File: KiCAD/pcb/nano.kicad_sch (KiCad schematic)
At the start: 24 parts, among them J1 Barrel_Jack_Switch, J2 Conn_01x02_Male, J3 Conn_01x02_Male, J4 Conn_01x04_Male, J5 Conn_01x03_Male, K1 SANYOU_SRD_Form_C, K2 SANYOU_SRD_Form_C, P1 Digital, P2 Analog, Q1 S8050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

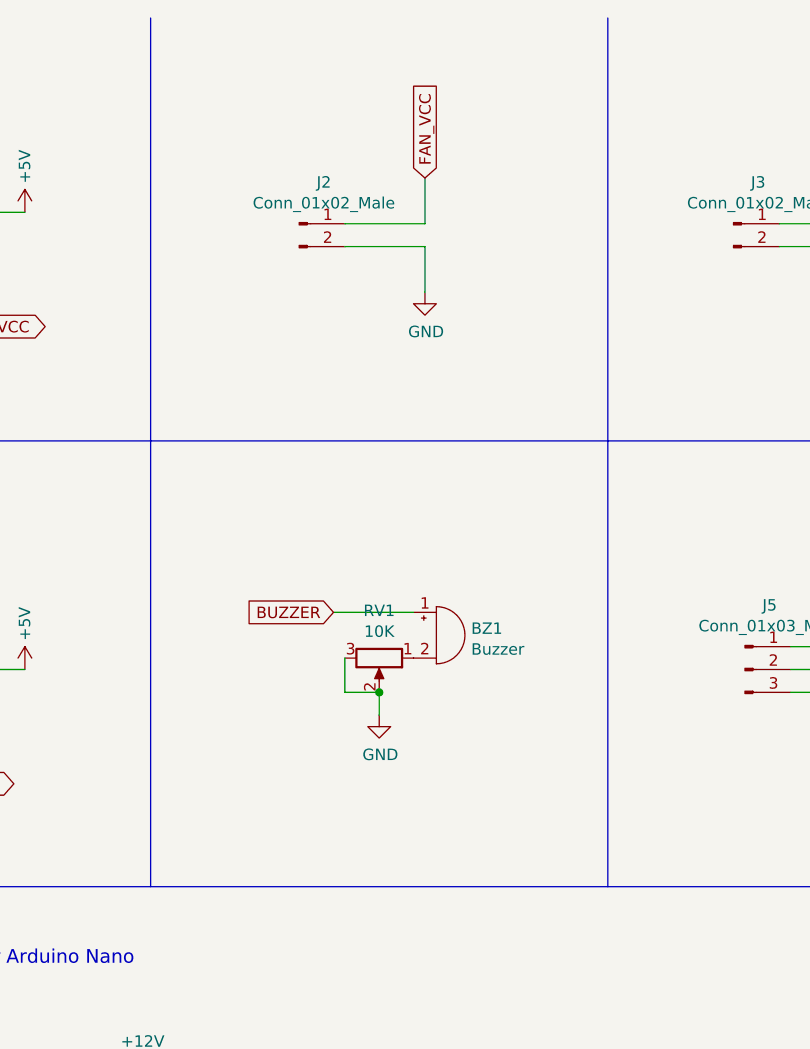
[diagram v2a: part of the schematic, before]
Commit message: added capacitor to fan
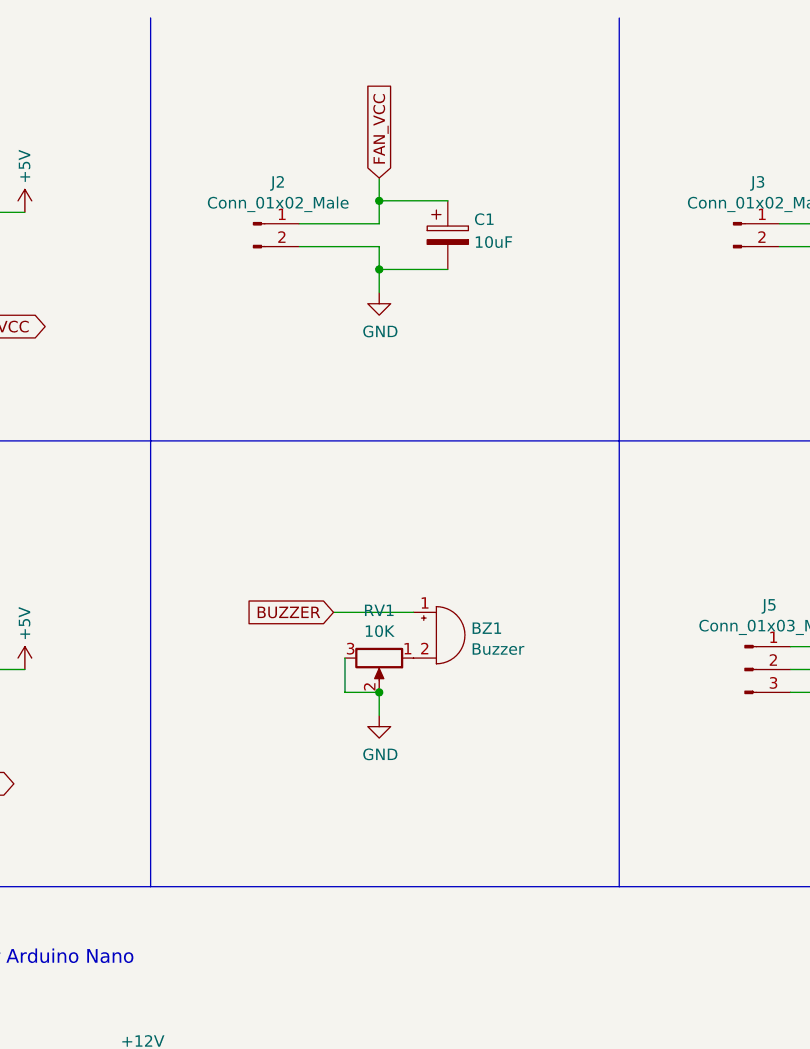
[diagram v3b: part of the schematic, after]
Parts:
- added C1: 10uF, Capacitor_THT:CP_Radial_D5.0mm_P2.00mm, symbol Device:C_Polarized
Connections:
- net FAN_VCC: now also C1.1
- net GND: now also C1.2
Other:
- moved on the sheet: J2
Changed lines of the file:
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@@
   (junction (at 88.9 34.29) (diameter 0) (color 0 0 0 0)
   )
+  (junction (at 134.62 33.02) (diameter 0) (color 0 0 0 0)
+  )
   (junction (at 63.5 72.39) (diameter 0) (color 0 0 0 0)
   )
@@
   )
   (junction (at 63.5 21.59) (diameter 0) (color 0 0 0 0)
+  )
+  (junction (at 134.62 40.64) (diameter 0) (color 0 0 0 0)
   )
   (no_connect (at 68.58 171.45))
@@
     (stroke (width 0) (type default) (color 0 0 0 0))
   )
-  (wire (pts (xy 139.7 38.1) (xy 139.7 43.18))
+  (wire (pts (xy 134.62 38.1) (xy 134.62 40.64))
     (stroke (width 0) (type default) (color 0 0 0 0))
   )
@@
     (stroke (width 0) (type default) (color 0 0 0 0))
   )
-  (wire (pts (xy 130.81 35.56) (xy 139.7 35.56))
+  (wire (pts (xy 134.62 40.64) (xy 134.62 43.18))
+    (stroke (width 0) (type default) (color 0 0 0 0))
+  )
+  (wire (pts (xy 125.73 35.56) (xy 134.62 35.56))
+    (stroke (width 0) (type default) (color 0 0 0 0))
+  )
+  (wire (pts (xy 134.62 33.02) (xy 134.62 30.48))
     (stroke (width 0) (type default) (color 0 0 0 0))
   )
@@
     (stroke (width 0) (type default) (color 0 0 0 0))
   )
-  (wire (pts (xy 139.7 35.56) (xy 139.7 30.48))
+  (wire (pts (xy 134.62 35.56) (xy 134.62 33.02))
     (stroke (width 0) (type default) (color 0 0 0 0))
   )
@@
     (stroke (width 0) (type default) (color 0 0 0 0))
   )
+  (wire (pts (xy 134.62 33.02) (xy 142.24 33.02))
+    (stroke (width 0) (type default) (color 0 0 0 0))
+  )
   (wire (pts (xy 199.39 134.62) (xy 199.39 130.81))
     (stroke (width 0) (type default) (color 0 0 0 0))
@@
     (stroke (width 0) (type default) (color 0 0 0 0))
   )
-  (wire (pts (xy 130.81 38.1) (xy 139.7 38.1))
+  (wire (pts (xy 125.73 38.1) (xy 134.62 38.1))
     (stroke (width 0) (type default) (color 0 0 0 0))
   )
@@
     (stroke (width 0) (type default) (color 0 0 0 0))
   )
-  (polyline (pts (xy 160.02 12.7) (xy 160.02 109.22))
+  (polyline (pts (xy 161.29 12.7) (xy 161.29 109.22))
     (stroke (width 0) (type default) (color 0 0 0 0))
   )
@@
   )
   (wire (pts (xy 85.09 146.05) (xy 50.8 146.05))
+    (stroke (width 0) (type default) (color 0 0 0 0))
+  )
+  (wire (pts (xy 134.62 40.64) (xy 142.24 40.64))
     (stroke (width 0) (type default) (color 0 0 0 0))
   )
@@
     (effects (font (size 0.635 0.635)) (justify left bottom))
   )
-  (global_label "FAN_VCC" (shape input) (at 139.7 30.48 90) (fields_autoplaced)
+  (global_label "FAN_VCC" (shape input) (at 134.62 30.48 90) (fields_autoplaced)
     (effects (font (size 1.27 1.27)) (justify left))
-    (property "Intersheet References" "${INTERSHEET_REFS}" (id 0) (at 0 0 0)
+    (property "Intersheet References" "${INTERSHEET_REFS}" (id 0) (at -5.08 0 0)
       (effects (font (size 1.27 1.27)) hide)
     )
@@
     (pin "1")
   )
-  (symbol (lib_id "Connector:Conn_01x02_Male") (at 125.73 35.56 0) (unit 1)
-    (in_bom yes) (on_board yes)
-    (property "Reference" "J2" (id 0) (at 128.4732 30.9626 0))
-    (property "Value" "Conn_01x02_Male" (id 1) (at 128.4732 33.274 0))
-    (property "Footprint" "Connector_JST:JST_XH_B2B-XH-AM_1x02_P2.50mm_Vertical" (id 2) (at 125.73 35.56 0)
-      (effects (font (size 1.27 1.27)) hide)
-    )
-    (property "Datasheet" "~" (id 3) (at 125.73 35.56 0)
+  (symbol (lib_id "Connector:Conn_01x02_Male") (at 120.65 35.56 0) (unit 1)
+    (in_bom yes) (on_board yes)
+    (property "Reference" "J2" (id 0) (at 123.3932 30.9626 0))
+    (property "Value" "Conn_01x02_Male" (id 1) (at 123.3932 33.274 0))
+    (property "Footprint" "Connector_JST:JST_XH_B2B-XH-AM_1x02_P2.50mm_Vertical" (id 2) (at 120.65 35.56 0)
+      (effects (font (size 1.27 1.27)) hide)
+    )
+    (property "Datasheet" "~" (id 3) (at 120.65 35.56 0)
       (effects (font (size 1.27 1.27)) hide)
     )
@@
     (pin "2")
   )
-  (symbol (lib_id "power:GND") (at 139.7 43.18 0) (unit 1)
-    (in_bom yes) (on_board yes)
-    (property "Reference" "#PWR010" (id 0) (at 139.7 49.53 0)
-      (effects (font (size 1.27 1.27)) hide)
-    )
-    (property "Value" "GND" (id 1) (at 139.827 47.5742 0))
-    (property "Footprint" "" (id 2) (at 139.7 43.18 0)
-      (effects (font (size 1.27 1.27)) hide)
-    )
-    (property "Datasheet" "" (id 3) (at 139.7 43.18 0)
+  (symbol (lib_id "power:GND") (at 134.62 43.18 0) (unit 1)
+    (in_bom yes) (on_board yes)
+    (property "Reference" "#PWR010" (id 0) (at 134.62 49.53 0)
+      (effects (font (size 1.27 1.27)) hide)
+    )
+    (property "Value" "GND" (id 1) (at 134.747 47.5742 0))
+    (property "Footprint" "" (id 2) (at 134.62 43.18 0)
+      (effects (font (size 1.27 1.27)) hide)
+    )
+    (property "Datasheet" "" (id 3) (at 134.62 43.18 0)
       (effects (font (size 1.27 1.27)) hide)
     )
@@
     (pin "1")
   )
+  (symbol (lib_id "Device:C_Polarized") (at 142.24 36.83 0) (unit 1)
+    (in_bom yes) (on_board yes) (fields_autoplaced)
+    (property "Reference" "C1" (id 0) (at 145.161 35.1063 0)
+      (effects (font (size 1.27 1.27)) (justify left))
+    )
+    (property "Value" "10uF" (id 1) (at 145.161 37.6432 0)
+      (effects (font (size 1.27 1.27)) (justify left))
+    )
+    (property "Footprint" "Capacitor_THT:CP_Radial_D5.0mm_P2.00mm" (id 2) (at 143.2052 40.64 0)
+      (effects (font (size 1.27 1.27)) hide)
+    )
+    (property "Datasheet" "~" (id 3) (at 142.24 36.83 0)
+      (effects (font (size 1.27 1.27)) hide)
+    )
+    (pin "1")
+    (pin "2")
+  )
   (symbol (lib_id "power:+5V") (at 95.25 34.29 0) (unit 1)
     (in_bom yes) (on_board yes)
@@
       (reference "BZ1") (unit 1) (value "Buzzer") (footprint "Buzzer_Beeper:Buzzer_12x9.5RM7.6")
     )
+    (path "/bf2004fc-ca2f-468b-b3d2-f793b64793d4"
+      (reference "C1") (unit 1) (value "10uF") (footprint "Capacitor_THT:CP_Radial_D5.0mm_P2.00mm")
+    )
     (path "/00000000-0000-0000-0000-000060df4020"

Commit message: 21-22 is better for starter
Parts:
- added C2: 1000uF, symbol Device:C_Polarized
- added D3: 1N4148, Diode_THT:D_DO-35_SOD27_P7.62mm_Horizontal, symbol Device:D
- added L1: 220, Inductor_SMD:L_7.3x7.3_H4.5, symbol Device:L
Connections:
- net +12V: now also C2.1
- net GND: now also C2.2
- net HEATER_VCC: now also D3.2 (A), L1.1; no longer J3.1 (Pin_1)
- new net: D3.1 (K), J3.1 (Pin_1), L1.2
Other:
- moved on the sheet: J3
